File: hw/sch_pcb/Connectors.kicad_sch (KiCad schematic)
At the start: 16 parts

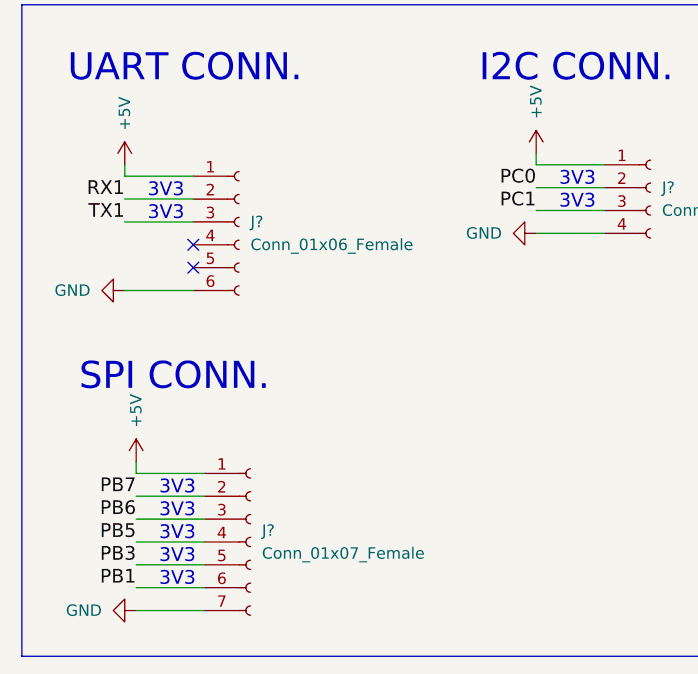
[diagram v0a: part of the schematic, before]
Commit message: schematics update - LTC4041, TPS631000
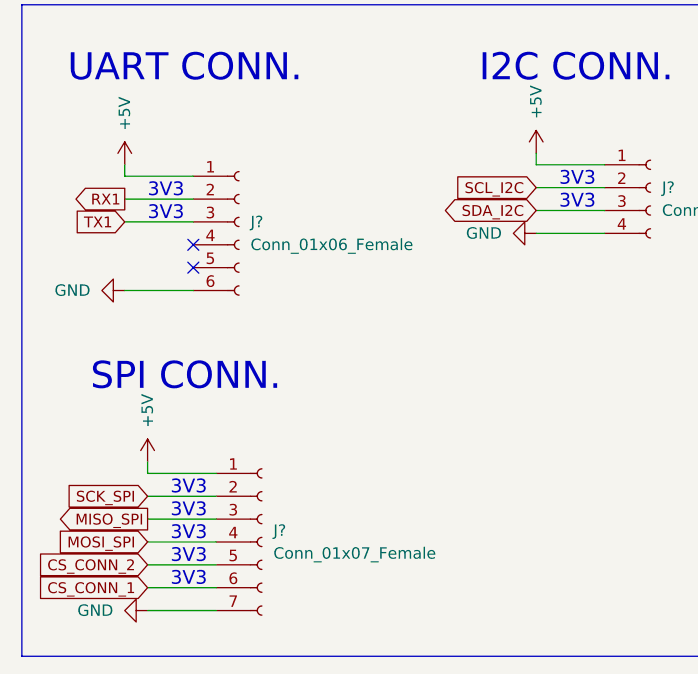
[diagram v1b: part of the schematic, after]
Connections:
- net PC0 is gone; now on net SCL_I2C: J?.2 (Pin_2)
- net PC1 is gone; now on net SDA_I2C: J?.3 (Pin_3)
- net PB1 renamed CS_CONN_1
- net PB3 renamed CS_CONN_2
- net PB5 renamed MOSI_SPI
- net PB6 renamed MISO_SPI
- net PB7 renamed SCK_SPI
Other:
- moved on the sheet: J?
